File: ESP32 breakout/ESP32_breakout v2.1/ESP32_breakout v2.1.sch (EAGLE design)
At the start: 37 parts, among them U1 ESP-WROOM-32, U2 NCP-1117, Y1 12MHz

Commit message: Traces
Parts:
- removed U$10: M04, dr-library:M04
- removed U$2: M102X05, dr-library:M102X05
- added U$3: M122ROWS, dr-library:M122ROWS
- R3: device dr-library:RESISTOR0603 -> dr-library:RESISTOR0805
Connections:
- net +3V3: no longer U$10.4
- net GND: no longer U$10.3
- net IO0/T1: now also U$3.1; no longer U$2.1
- net IO16: now also U$3.3; no longer U$2.3
- net IO17: now also U$3.4; no longer U$2.4
- net IO18: now also U$3.6; no longer U$2.6
- net IO19: now also U$3.7; no longer U$2.7
- net IO21: now also U$3.8; no longer U$2.8
- net IO22: now also U$3.11; no longer U$2.9
- net IO23: now also U$3.12; no longer U$2.10
- net IO4/T0: now also U$3.2; no longer U$2.2
- net IO5: now also U$3.5; no longer U$2.5
- net RX: now also U$3.9; no longer U$10.1
- net TX: now also U$3.10; no longer U$10.2
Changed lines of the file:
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@@
 <part name="+3V3" library="supply1" deviceset="+3V3" device=""/>
 <part name="D1" library="dr-library" deviceset="LED" device="1206"/>
-<part name="R3" library="dr-library" deviceset="RESISTOR" device="0603" value="330"/>
+<part name="R3" library="dr-library" deviceset="RESISTOR" device="0805" value="330"/>
 <part name="+3V4" library="supply1" deviceset="+3V3" device=""/>
 <part name="GND6" library="supply1" deviceset="GND" device=""/>
@@
 <part name="U$17" library="dr-library" deviceset="M10" device="2X05"/>
 <part name="U$5" library="dr-library" deviceset="M10" device="2X05"/>
-<part name="U$2" library="dr-library" deviceset="M10" device="2X05"/>
-<part name="U$10" library="dr-library" deviceset="M04" device=""/>
 <part name="C10" library="dr-library" deviceset="TOUCHPAD" device="-10MMX10MM" value="TOUCHPAD-10MMX10MM"/>
 <part name="C11" library="dr-library" deviceset="TOUCHPAD" device="-10MMX10MM" value="TOUCHPAD-10MMX10MM"/>
@@
 <part name="C16" library="dr-library" deviceset="TOUCHPAD" device="-10MMX10MM" value="TOUCHPAD-10MMX10MM"/>
 <part name="C17" library="dr-library" deviceset="TOUCHPAD" device="-10MMX10MM" value="TOUCHPAD-10MMX10MM"/>
+<part name="U$3" library="dr-library" deviceset="M12" device="2ROWS"/>
 </parts>
 <sheets>
@@
 <instance part="U$17" gate="G$1" x="93.98" y="2.54" rot="R180"/>
 <instance part="U$5" gate="G$1" x="187.96" y="2.54" rot="R180"/>
-<instance part="U$2" gate="G$1" x="215.9" y="-2.54" rot="R180"/>
-<instance part="U$10" gate="G$1" x="187.96" y="-27.94" rot="R180"/>
 <instance part="C10" gate="G$1" x="-30.48" y="33.02" rot="R180"/>
 <instance part="C11" gate="G$1" x="-30.48" y="25.4" rot="R180"/>
@@
 <instance part="C16" gate="G$1" x="-30.48" y="-12.7" rot="R180"/>
 <instance part="C17" gate="G$1" x="-30.48" y="-20.32" rot="R180"/>
+<instance part="U$3" gate="G$1" x="137.16" y="0" rot="R180"/>
 </instances>
 <busses>
@@
 <wire x1="182.88" y1="-30.48" x2="175.26" y2="-30.48" width="0.1524" layer="91"/>
 <label x="175.26" y="-30.48" size="1.778" layer="95"/>
-<pinref part="U$10" gate="G$1" pin="3"/>
 </segment>
 </net>
@@
 <wire x1="182.88" y1="-27.94" x2="175.26" y2="-27.94" width="0.1524" layer="91"/>
 <label x="175.26" y="-27.94" size="1.778" layer="95"/>
-<pinref part="U$10" gate="G$1" pin="4"/>
 </segment>
 </net>
@@
 <wire x1="132.08" y1="5.08" x2="124.46" y2="5.08" width="0.1524" layer="91"/>
 <label x="124.46" y="5.08" size="1.778" layer="95" font="vector"/>
+<pinref part="U$3" gate="G$1" pin="10"/>
 </segment>
 <segment>
@@
 <label x="175.26" y="-33.02" size="1.778" layer="95"/>
 <label x="175.26" y="-33.02" size="1.778" layer="95"/>
-<pinref part="U$10" gate="G$1" pin="2"/>
 </segment>
 </net>
@@
 <wire x1="132.08" y1="2.54" x2="124.46" y2="2.54" width="0.1524" layer="91"/>
 <label x="124.46" y="2.54" size="1.778" layer="95" font="vector"/>
+<pinref part="U$3" gate="G$1" pin="9"/>
 </segment>
 <segment>
@@
 <wire x1="182.88" y1="-35.56" x2="175.26" y2="-35.56" width="0.1524" layer="91"/>
 <label x="175.26" y="-35.56" size="1.778" layer="95"/>
-<pinref part="U$10" gate="G$1" pin="1"/>
 </segment>
 </net>
@@
 <wire x1="132.08" y1="-15.24" x2="124.46" y2="-15.24" width="0.1524" layer="91"/>
 <label x="124.46" y="-15.24" size="1.778" layer="95" font="vector"/>
+<pinref part="U$3" gate="G$1" pin="2"/>
 </segment>
 <segment>
 <wire x1="210.82" y1="-17.78" x2="203.2" y2="-17.78" width="0.1524" layer="91"/>
 <label x="203.2" y="-17.78" size="1.778" layer="95" font="vector"/>
-<pinref part="U$2" gate="G$1" pin="2"/>
 </segment>
 <segment>
@@
 <wire x1="132.08" y1="-7.62" x2="124.46" y2="-7.62" width="0.1524" layer="91"/>
 <label x="124.46" y="-7.62" size="1.778" layer="95" font="vector"/>
+<pinref part="U$3" gate="G$1" pin="5"/>
 </segment>
 <segment>
 <wire x1="210.82" y1="-10.16" x2="203.2" y2="-10.16" width="0.1524" layer="91"/>
 <label x="203.2" y="-10.16" size="1.778" layer="95" font="vector"/>
-<pinref part="U$2" gate="G$1" pin="5"/>
 </segment>
 </net>
@@
 <wire x1="132.08" y1="-5.08" x2="124.46" y2="-5.08" width="0.1524" layer="91"/>
 <label x="124.46" y="-5.08" size="1.778" layer="95" font="vector"/>
+<pinref part="U$3" gate="G$1" pin="6"/>
 </segment>
 <segment>
 <wire x1="210.82" y1="-7.62" x2="203.2" y2="-7.62" width="0.1524" layer="91"/>
 <label x="203.2" y="-7.62" size="1.778" layer="95" font="vector"/>
-<pinref part="U$2" gate="G$1" pin="6"/>
 </segment>
 </net>
@@
 <wire x1="132.08" y1="-2.54" x2="124.46" y2="-2.54" width="0.1524" layer="91"/>
 <label x="124.46" y="-2.54" size="1.778" layer="95" font="vector"/>
+<pinref part="U$3" gate="G$1" pin="7"/>
 </segment>
 <segment>
 <wire x1="210.82" y1="-5.08" x2="203.2" y2="-5.08" width="0.1524" layer="91"/>
 <label x="203.2" y="-5.08" size="1.778" layer="95" font="vector"/>
-<pinref part="U$2" gate="G$1" pin="7"/>
 </segment>
 </net>
@@
 <wire x1="132.08" y1="0" x2="124.46" y2="0" width="0.1524" layer="91"/>
 <label x="124.46" y="0" size="1.778" layer="95" font="vector"/>
+<pinref part="U$3" gate="G$1" pin="8"/>
 </segment>
 <segment>
 <wire x1="210.82" y1="-2.54" x2="203.2" y2="-2.54" width="0.1524" layer="91"/>
 <label x="203.2" y="-2.54" size="1.778" layer="95" font="vector"/>
-<pinref part="U$2" gate="G$1" pin="8"/>
 </segment>
 </net>
@@
 <wire x1="132.08" y1="7.62" x2="124.46" y2="7.62" width="0.1524" layer="91"/>
 <label x="124.46" y="7.62" size="1.778" layer="95" font="vector"/>
+<pinref part="U$3" gate="G$1" pin="11"/>
 </segment>
 <segment>
 <wire x1="210.82" y1="0" x2="203.2" y2="0" width="0.1524" layer="91"/>
 <label x="203.2" y="0" size="1.778" layer="95" font="vector"/>
-<pinref part="U$2" gate="G$1" pin="9"/>
 </segment>
 </net>
@@
 <wire x1="132.08" y1="10.16" x2="124.46" y2="10.16" width="0.1524" layer="91"/>
 <label x="124.46" y="10.16" size="1.778" layer="95" font="vector"/>
+<pinref part="U$3" gate="G$1" pin="12"/>
 </segment>
 <segment>
 <wire x1="210.82" y1="2.54" x2="203.2" y2="2.54" width="0.1524" layer="91"/>
 <label x="203.2" y="2.54" size="1.778" layer="95" font="vector"/>
-<pinref part="U$2" gate="G$1" pin="10"/>
 </segment>
 </net>
@@
 <wire x1="132.08" y1="-10.16" x2="124.46" y2="-10.16" width="0.1524" layer="91"/>
 <label x="124.46" y="-10.16" size="1.778" layer="95" font="vector"/>
+<pinref part="U$3" gate="G$1" pin="4"/>
 </segment>
 <segment>
 <wire x1="210.82" y1="-12.7" x2="203.2" y2="-12.7" width="0.1524" layer="91"/>
 <label x="203.2" y="-12.7" size="1.778" layer="95" font="vector"/>
-<pinref part="U$2" gate="G$1" pin="4"/>
 </segment>
 </net>
@@
 <wire x1="132.08" y1="-12.7" x2="124.46" y2="-12.7" width="0.1524" layer="91"/>
 <label x="124.46" y="-12.7" size="1.778" layer="95" font="vector"/>
+<pinref part="U$3" gate="G$1" pin="3"/>
 </segment>
 <segment>
 <wire x1="210.82" y1="-15.24" x2="203.2" y2="-15.24" width="0.1524" layer="91"/>
 <label x="203.2" y="-15.24" size="1.778" layer="95" font="vector"/>
-<pinref part="U$2" gate="G$1" pin="3"/>
 </segment>
 </net>
@@
 <wire x1="132.08" y1="-17.78" x2="124.46" y2="-17.78" width="0.1524" layer="91"/>
 <label x="124.46" y="-17.78" size="1.778" layer="95" font="vector"/>
+<pinref part="U$3" gate="G$1" pin="1"/>
 </segment>
 <segment>
 <wire x1="210.82" y1="-20.32" x2="203.2" y2="-20.32" width="0.1524" layer="91"/>
 <label x="203.2" y="-20.32" size="1.778" layer="95" font="vector"/>
-<pinref part="U$2" gate="G$1" pin="1"/>
-</segment>
-<segment>
+</segment>
+<segment>

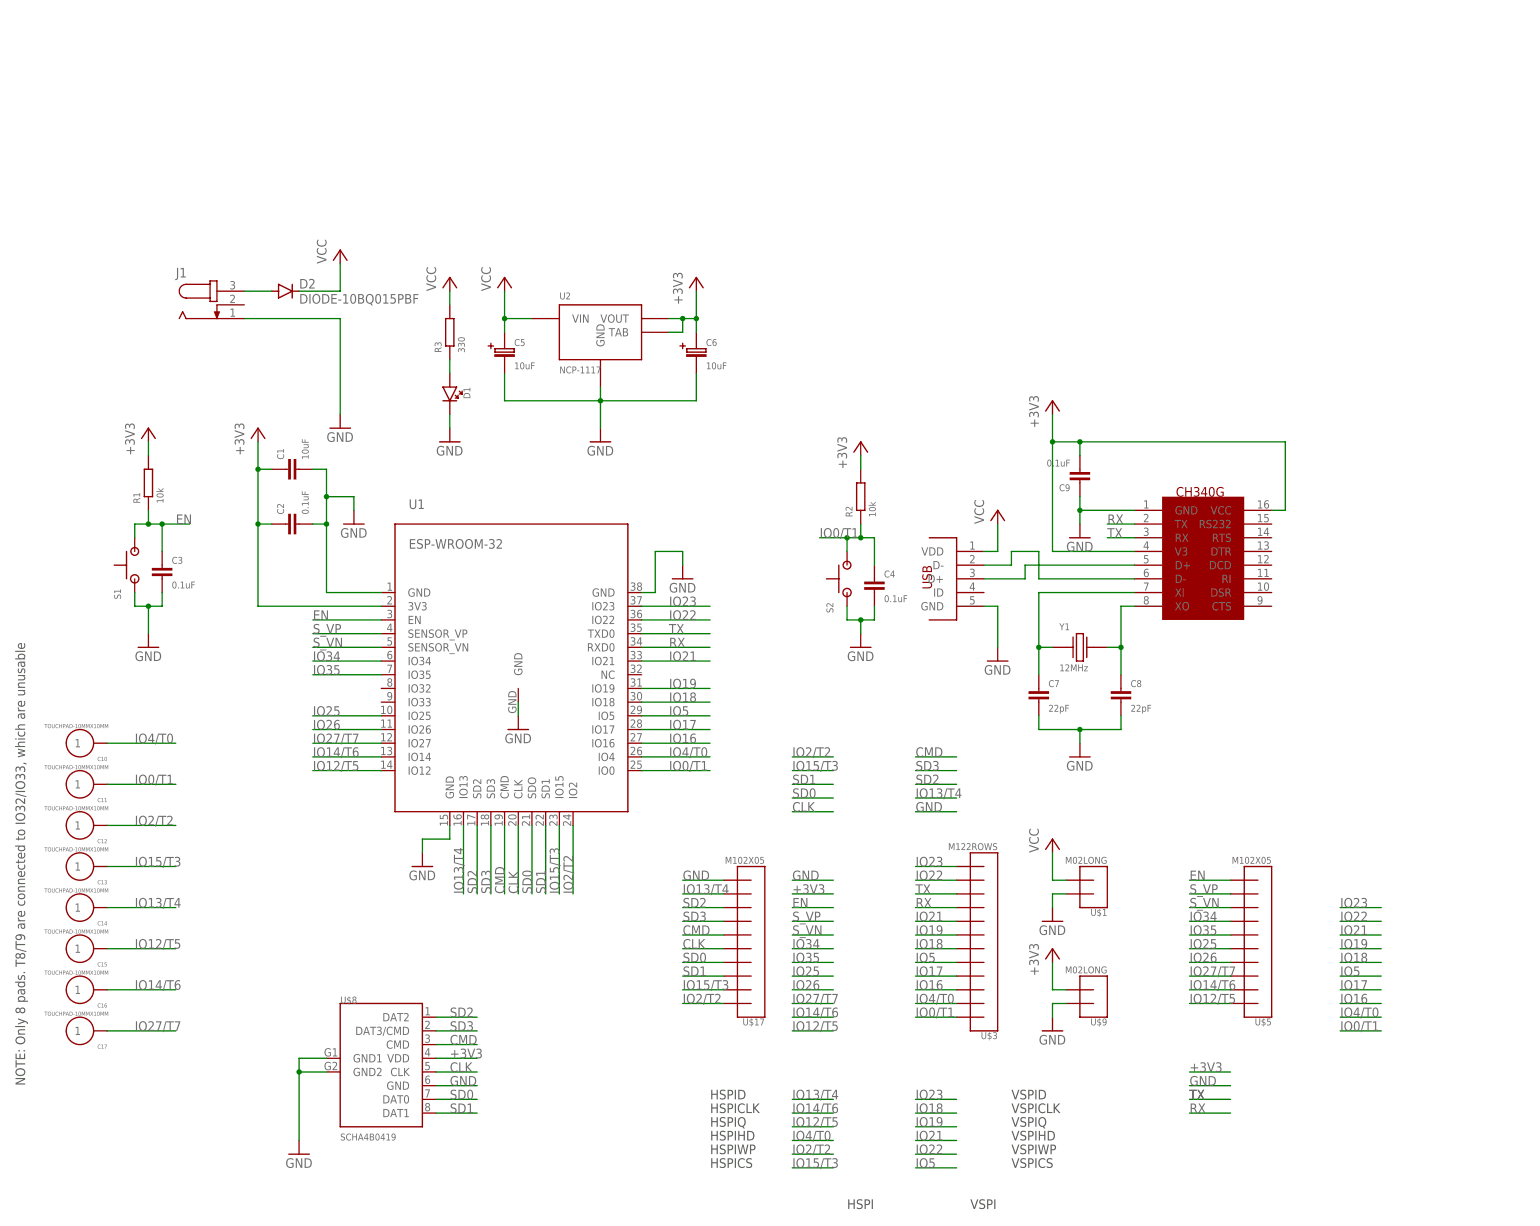
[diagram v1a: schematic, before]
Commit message: Added more status LEDs
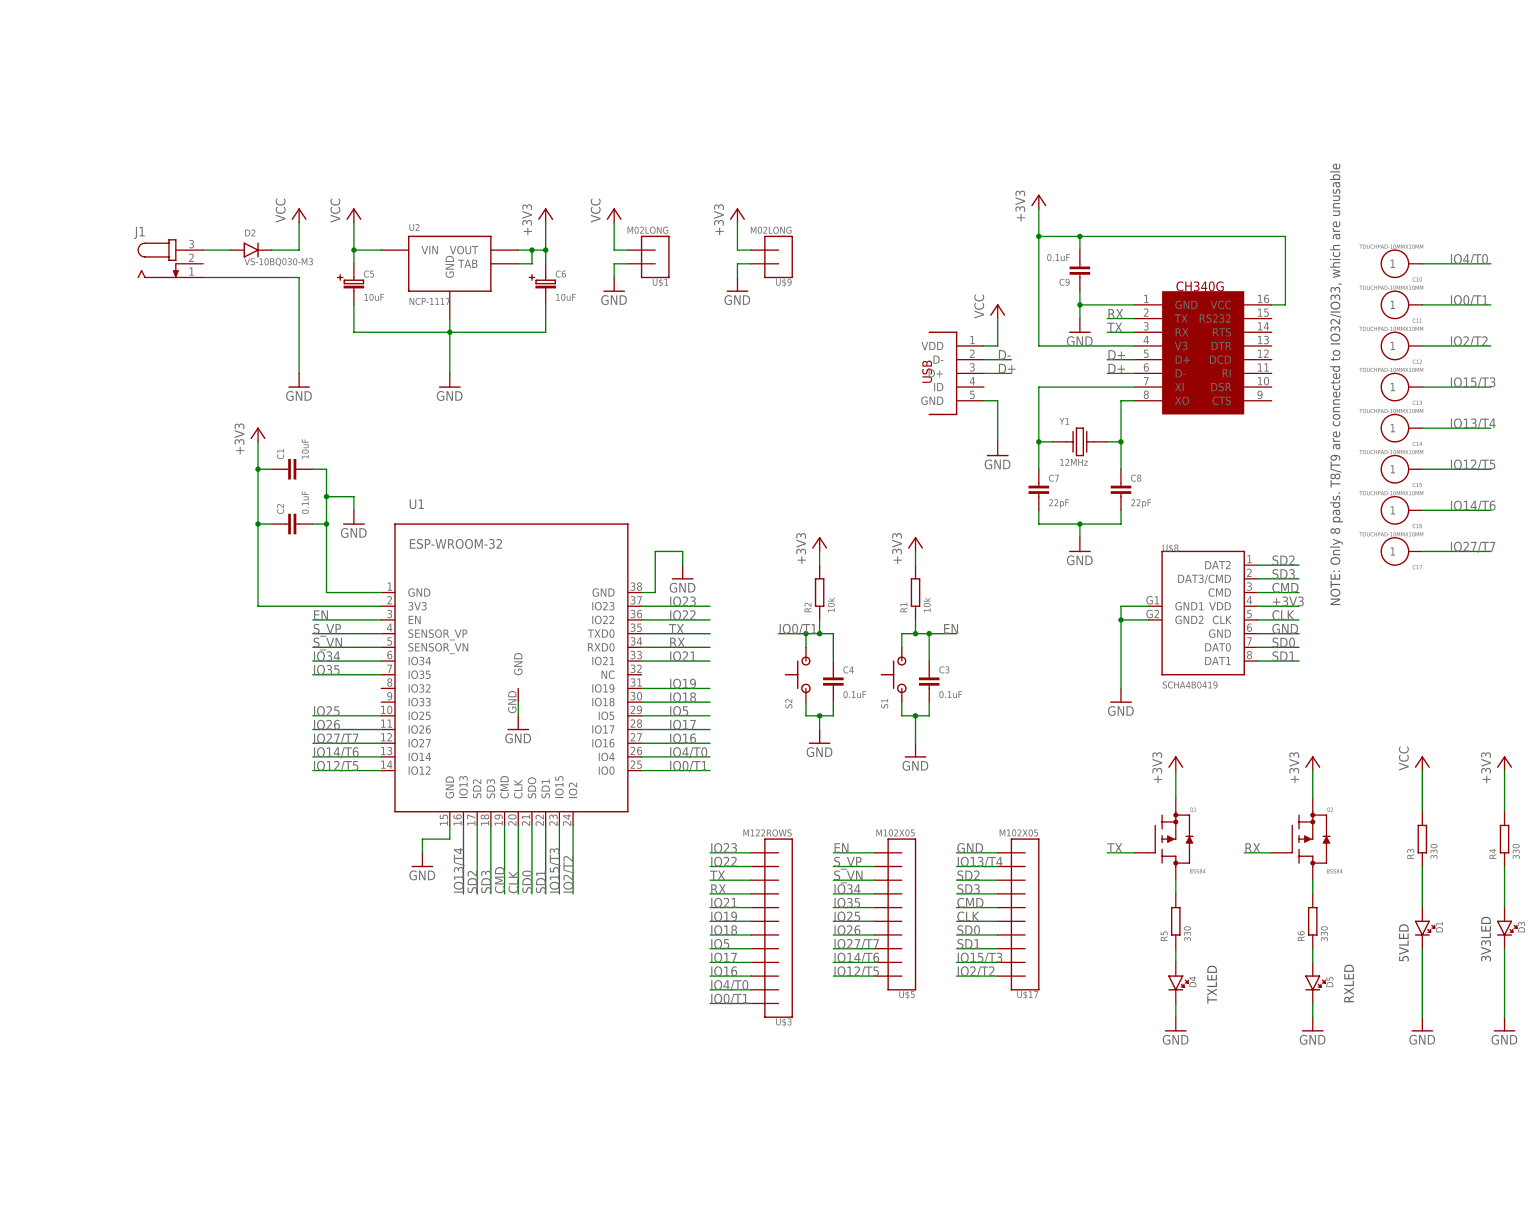
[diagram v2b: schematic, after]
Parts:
- added D3, D4, D5: (no value), dr-library:LED1206
- added Q1, Q2: BSS84, dr-library:BSS84
- added R4, R5, R6: 330, dr-library:RESISTOR0805
- D2: value DIODE-10BQ015PBF -> VS-10BQ030-M3; device EmbeddedAdventures 3:DIODE-10BQ015PBF -> dr-library:VS-10BQ030-M3
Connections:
- net N$5 renamed D+
- net N$6 renamed D-
- new net N$11: D5.A, R6.1
- new net N$5: D3.A, R4.1
- new net N$6: Q1.D, R5.2
- new net N$7: Q2.D, R6.2
- new net N$8: D4.A, R5.1
- net +3V3: now also Q1.S, Q2.S, R4.2
- net GND: now also D3.C, D4.C, D5.C
- net RX: now also Q2.G
- net TX: now also Q1.G
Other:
- note added: "3V3LED"
- note added: "5VLED"
- note added: "RXLED"
- note added: "TXLED"
- note removed: "HSPI"
- note removed: "HSPICLK"
- note removed: "HSPICS"
- note removed: "HSPID"
- note removed: "HSPIHD"
- note removed: "HSPIQ"
- note removed: "HSPIWP"
- note removed: "VSPI"
- note removed: "VSPICLK"
- note removed: "VSPICS"
- note removed: "VSPID"
- note removed: "VSPIHD"
- note removed: "VSPIQ"
- note removed: "VSPIWP"
- moved on the sheet: C10, C11, C12, C13, C14, C15, C16, C17, C3, C4, C5, C6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

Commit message: Added USB bypass cap and extra status LED
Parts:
- added C18: 0.1uF, dr-library:CAP0603
- added D6: (no value), dr-library:LED1206
- added J2: JUMPER_2-WAY, dr-library:JUMPER_2-WAY
- added Q3: BSS84, dr-library:BSS84
- added R7: 330, dr-library:RESISTOR0805
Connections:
- new net HEART: J2.1, Q3.G
- new net N$10: Q3.D, R7.2
- new net N$9: D6.A, R7.1
- net +3V3: now also Q3.S
- net GND: now also C18.2, D6.C
- net IO19: now also J2.2
- net VCC: now also C18.1
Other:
- note added: "Breakout Header"
- note added: "ESP32 Module"
- note added: "HEARTBEAT"
- note added: "MicroSD"
- note added: "Name: David Rances"
- note added: "Power"
- note added: "Status LEDs"
- note added: "Touch Pad"
- note added: "USB-UART"
- moved on the sheet: C1, C10, C11, C12, C13, C14, C15, C16, C17, C2, C3, C4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
